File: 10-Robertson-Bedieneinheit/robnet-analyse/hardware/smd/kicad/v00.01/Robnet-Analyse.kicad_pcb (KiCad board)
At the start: 2 copper layers, 100 x 100 mm, 71 parts, among them J1 MSTBA 6-pol., J2 MSTBA 2-pol., J3 MSTBA 6-pol., J4 Messpunkte, J5 Raspberry Pi Zero 2 W, U1 MAX3488EEPA, U2 MCP3208-CI/P, U3 R-78B5.0-2.0, U4 LM4040AIZ-2.5, U6 MCP3208-CI/P

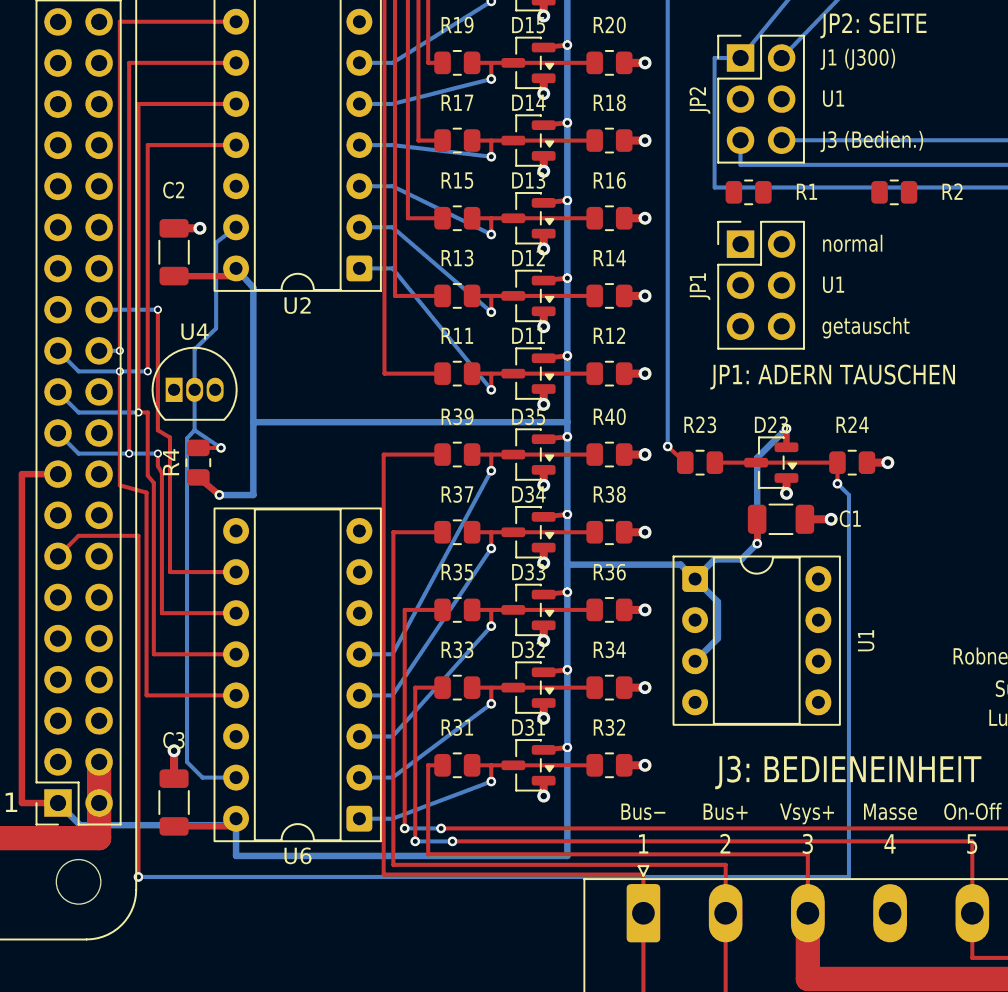
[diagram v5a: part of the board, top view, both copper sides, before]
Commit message: Robnet-Analyse Linie B: Leiterbahnen Gruppe 5 (Empfaenger), Platine vollstaendig verlegt
- Bahnen 00.05: JP2 -> R1/R2 -> JP1 (Kreuzung Bus+ unten, Bus- oben), A/B zu U1,
  Empfaengerleitung zum Zero Pin 10 und 16; Alarm und Empfaenger links von J3
  tiefer (Masseflaeche ein Stueck)
- Keine offene Verbindung, DRC ohne Fehler, Abgleich 0, 79 Durchkontaktierungen
- Konzept 00.43, Bauteilauswahl SMD 00.15

Co-Authored-By: Claude Opus 5.5 <noreply@anthropic.com>
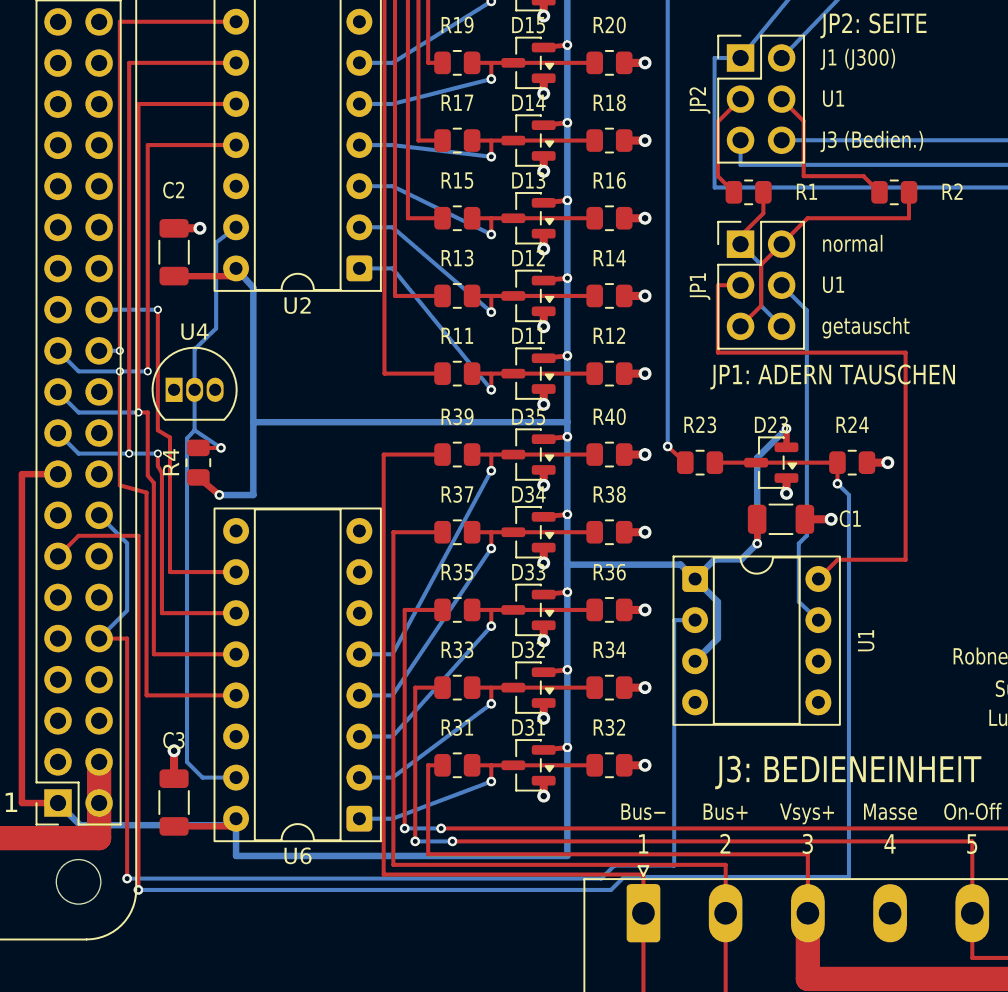
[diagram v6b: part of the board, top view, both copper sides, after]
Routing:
- net /Bus-Empfänger/BUS_RX: track 0.00 -> 76.2 mm, vias 0 -> 1
- net Net-(JP1-A): track 0.00 -> 35.8 mm
- net Net-(JP1-B): track 0.00 -> 22.1 mm
- net Net-(JP1-Bus−-Pad2): track 0.00 -> 16.3 mm
- net Net-(JP2-Bus−): track 0.00 -> 10.4 mm
- net Net-(JP1-Bus+-Pad1): track 0.00 -> 9.92 mm
- net Net-(JP2-Bus+): track 0.00 -> 6.75 mm
- net /Messung (Teiler, Wandler)/ALARM_ZERO: track 104.0 -> 105.1 mm
